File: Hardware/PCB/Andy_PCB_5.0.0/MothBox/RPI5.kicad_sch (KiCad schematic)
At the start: 4 parts, among them U16 Female Inv Socket Pi 2.54-2*20, U18 RASPBERRY_PI_4B_4GB, U4 RASPBERRY_PI_4B_4GB, U5 RASPBERRY_PI_5

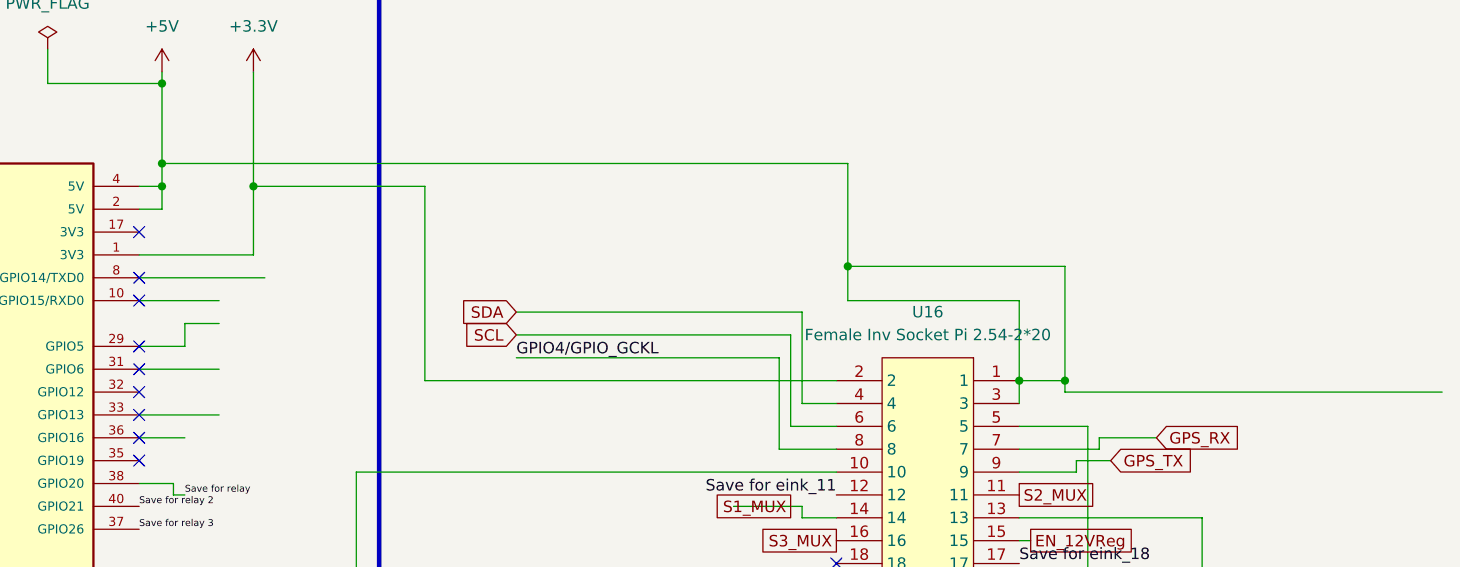
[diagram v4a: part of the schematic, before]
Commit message: Fixed parts with conflicting LCSC footprints
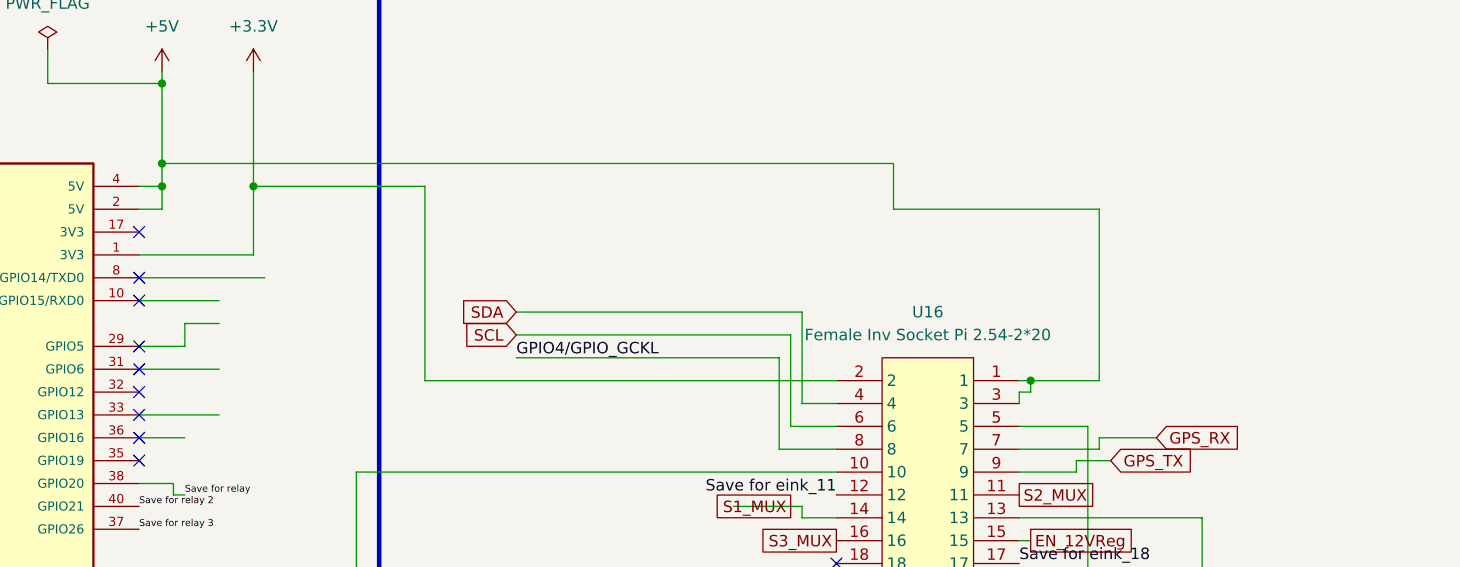
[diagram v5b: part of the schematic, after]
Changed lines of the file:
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@@
-	)
-	(junction
-		(at 175.26 49.53)
-		(diameter 0)
-		(color 0 0 0 0)
 	)
 	(junction
@@
 	)
 	(junction
-		(at 199.39 62.23)
-		(diameter 0)
-		(color 0 0 0 0)
-	)
-	(junction
-		(at 194.31 62.23)
+		(at 195.58 62.23)
 		(diameter 0)
 		(color 0 0 0 0)
@@
 	(wire
 		(pts
+			(xy 195.58 62.23) (xy 194.31 62.23)
+		)
+		(stroke
+			(width 0)
+			(type default)
+		)
+	)
+	(wire
+		(pts
 			(xy 170.18 76.2) (xy 170.18 77.47)
 		)
@@
 	(wire
 		(pts
-			(xy 199.39 49.53) (xy 199.39 62.23)
-		)
-		(stroke
-			(width 0)
-			(type default)
-		)
-	)
-	(wire
-		(pts
 			(xy 101.6 74.93) (xy 100.33 74.93)
 		)
@@
 	(wire
 		(pts
+			(xy 194.31 63.5) (xy 194.31 64.77)
+		)
+		(stroke
+			(width 0)
+			(type default)
+		)
+	)
+	(wire
+		(pts
 			(xy 100.33 105.41) (xy 102.87 105.41)
 		)
@@
 	(wire
 		(pts
-			(xy 194.31 53.34) (xy 175.26 53.34)
+			(xy 203.2 43.18) (xy 180.34 43.18)
 		)
 		(stroke
@@
 	(wire
 		(pts
-			(xy 175.26 49.53) (xy 175.26 53.34)
+			(xy 180.34 38.1) (xy 180.34 43.18)
 		)
 		(stroke
@@
 	(wire
 		(pts
-			(xy 241.3 63.5) (xy 199.39 63.5)
-		)
-		(stroke
-			(width 0)
-			(type default)
-		)
-	)
-	(wire
-		(pts
 			(xy 109.22 40.64) (xy 128.27 40.64)
 		)
@@
 	(wire
 		(pts
-			(xy 199.39 62.23) (xy 194.31 62.23)
-		)
-		(stroke
-			(width 0)
-			(type default)
-		)
-	)
-	(wire
-		(pts
 			(xy 120.65 72.39) (xy 120.65 106.68)
 		)
@@
 	(wire
 		(pts
-			(xy 199.39 49.53) (xy 175.26 49.53)
+			(xy 203.2 62.23) (xy 195.58 62.23)
 		)
 		(stroke
@@
 	(wire
 		(pts
-			(xy 194.31 62.23) (xy 194.31 64.77)
+			(xy 195.58 62.23) (xy 195.58 63.5)
 		)
 		(stroke
@@
 	(wire
 		(pts
-			(xy 175.26 38.1) (xy 99.06 38.1)
+			(xy 180.34 38.1) (xy 99.06 38.1)
 		)
 		(stroke
@@
 	(wire
 		(pts
-			(xy 194.31 53.34) (xy 194.31 62.23)
+			(xy 203.2 43.18) (xy 203.2 62.23)
 		)
 		(stroke
@@
 	(wire
 		(pts
-			(xy 175.26 49.53) (xy 175.26 38.1)
+			(xy 195.58 63.5) (xy 194.31 63.5)
 		)
 		(stroke
@@
 		)
 		(stroke
-			(width 0)
-			(type default)
-		)
-	)
-	(wire
-		(pts
-			(xy 199.39 62.23) (xy 199.39 63.5)
-		)
-		(stroke

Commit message: Final changes footprints before JLC
c1 - rotate left 180

e3 - rotate left 180

q1 rotate l 180

U1,U2,U6,U7 rotate 180

u5 Epaper header - 90 right

u16 - NOT RIGHT ANGLE should be C2897440  or C22373943
d30 they might be bidirectional

Q10,Q11,Q4,Q6,Q8,Q9

C39828
rotate 180
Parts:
- U16: LCSC Part C2977589 -> C2897440
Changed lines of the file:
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@@
 	)
 	(symbol
+		(lib_name "RASPBERRY_PI_4B_4GB_2")
 		(lib_id "RASPBERRY_PI_4B_4GB:RASPBERRY_PI_4B_4GB")
 		(at 71.12 71.12 0)
@@
 			)
 		)
-		(property "LCSC Part" "C2977589"
+		(property "LCSC Part" "C2897440"
 			(at 184.15 120.65 0)
 			(effects

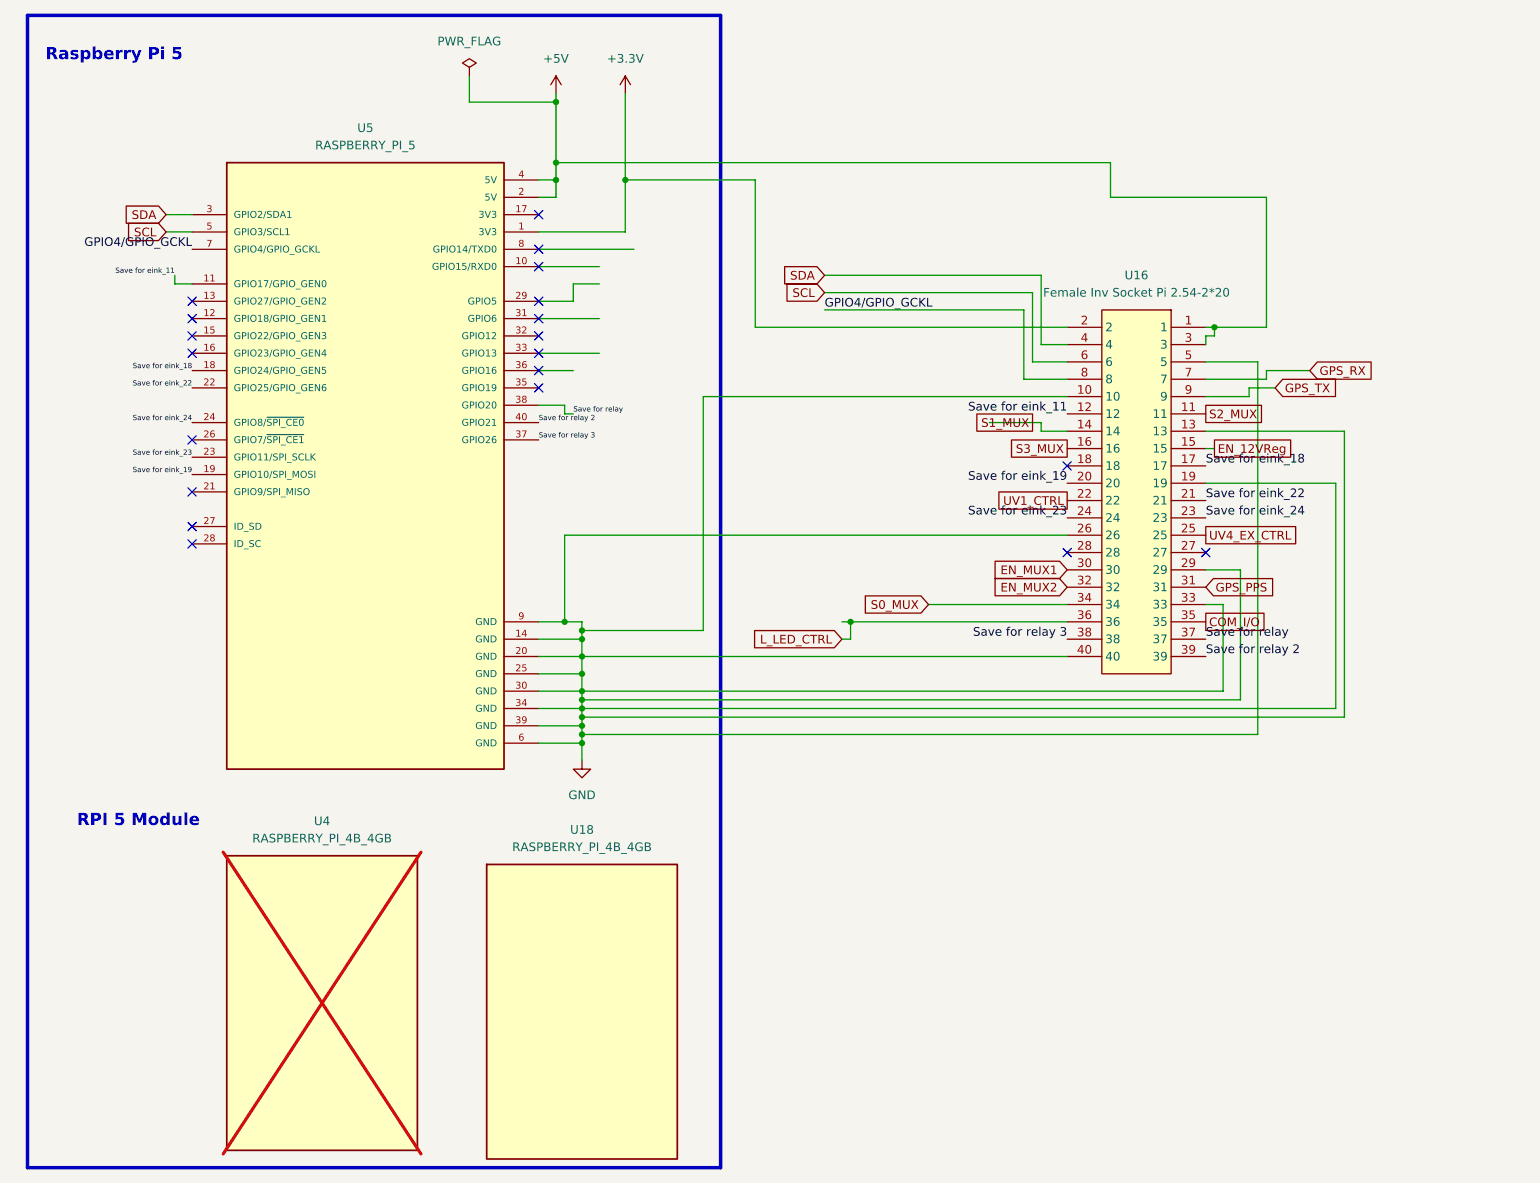
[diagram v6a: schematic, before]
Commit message: Switched from Analog Muxers to Shift Registers
Freed up 3 pins on the RasPi
Using 4 pins
SHIFT LOAD
SHIFT CLOCK
SHIFT DATA
SWITCH ENABLE
The Switch Enable pin drives +V to the switch array so it's not 'on' all the time

These hardware changes require changes to the code base
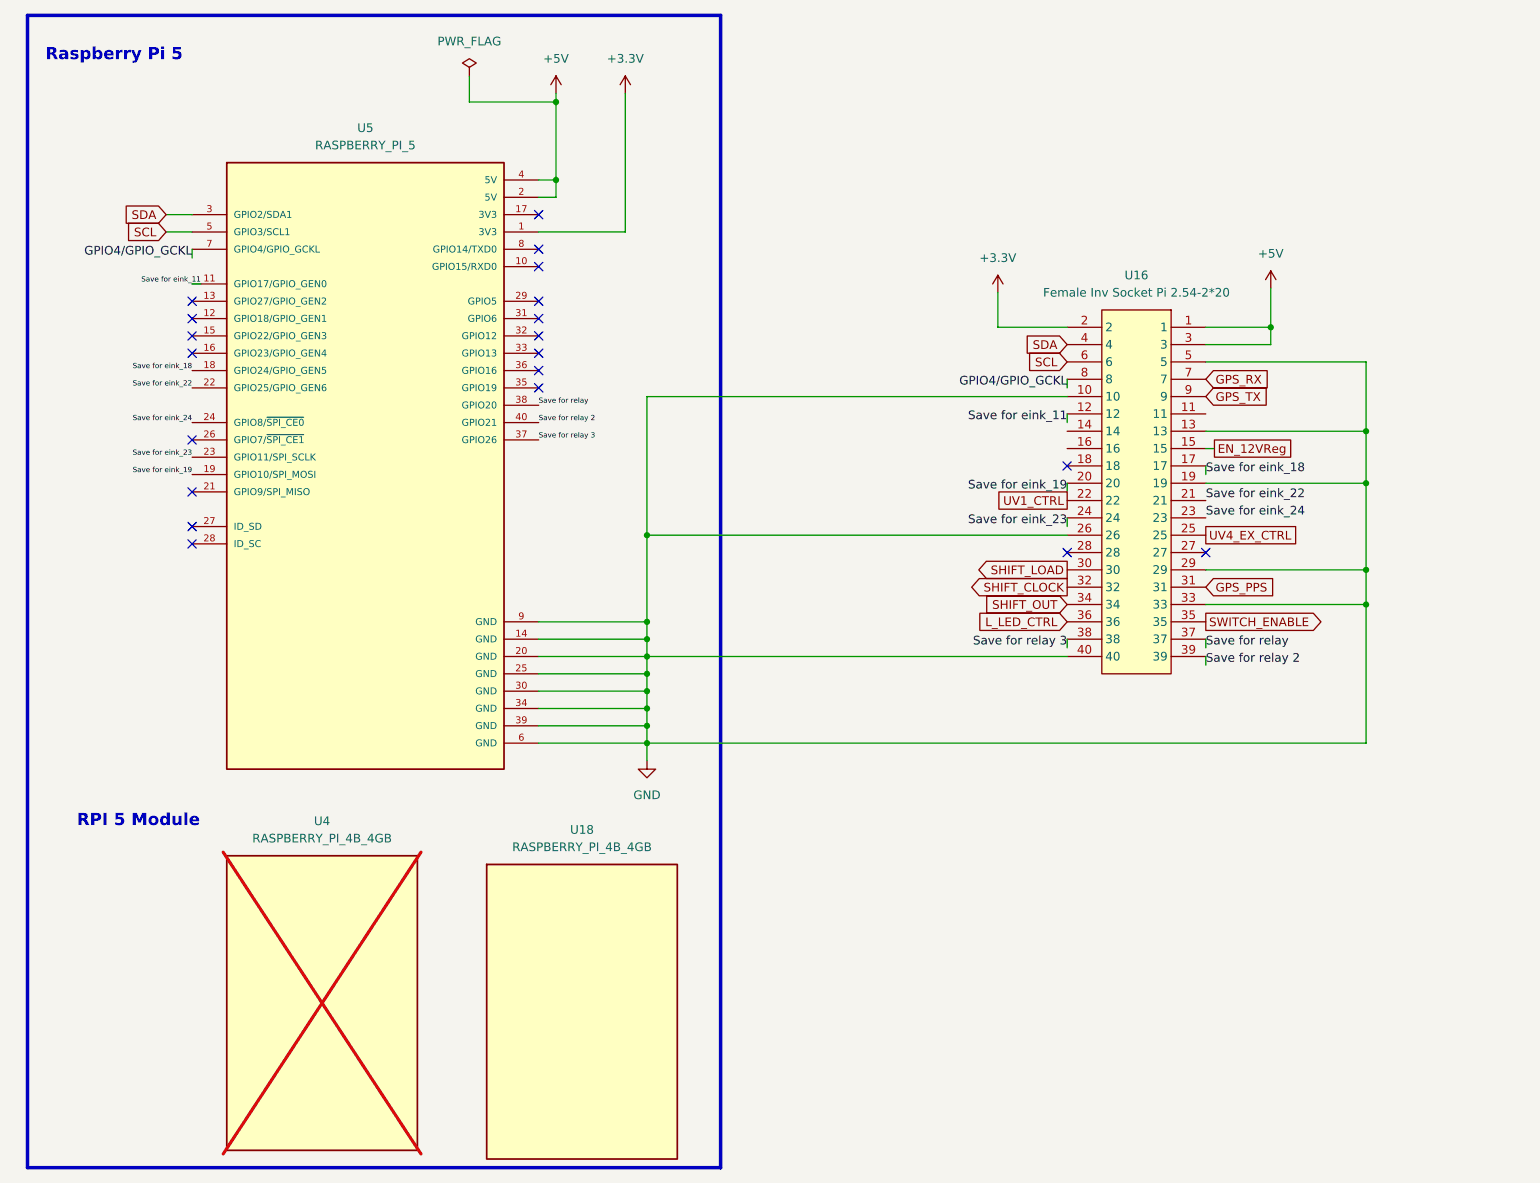
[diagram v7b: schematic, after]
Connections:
- net COM_I/O renamed SWITCH_ENABLE
- net EN_MUX1 renamed SHIFT_LOAD
- net EN_MUX2 renamed SHIFT_CLOCK
- net S0_MUX renamed SHIFT_OUT
- net S1_MUX: no longer names the net of U16.14
- net S2_MUX: no longer names the net of U16.11
- net S3_MUX: no longer names the net of U16.16
